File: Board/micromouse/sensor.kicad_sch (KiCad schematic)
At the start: 9 parts, among them Q1 DMN63D8L-7

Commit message: レビュー対応
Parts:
- C4: value 0.1u -> 0.01u
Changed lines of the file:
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@@
       (effects (font (size 1.27 1.27)))
     )
-    (property "Value" "0.1u" (at 163.83 93.98 90)
+    (property "Value" "0.01u" (at 163.83 93.98 90)
       (effects (font (size 1.27 1.27)))
     )

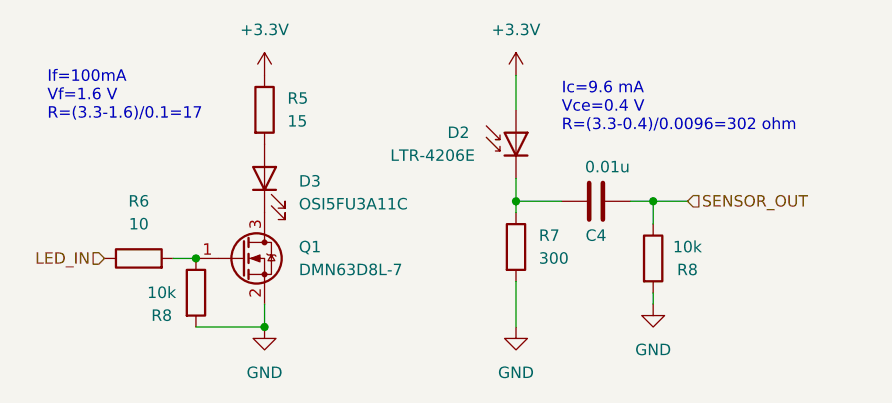
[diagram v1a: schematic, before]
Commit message: 部品型番、URLを追加
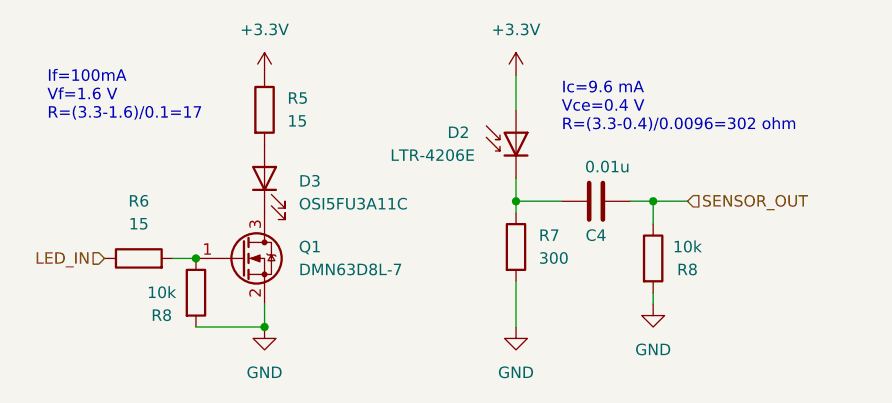
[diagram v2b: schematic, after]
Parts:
- C4: manf# (none) -> GCM155R71H103KA55D; order_URL (none) -> https://www.digikey.jp/ja/products/detail/murata-electronic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
- D2: manf# (none) -> LTR-4206E
- D3: manf# (none) -> OSI5FU3A11C
- R5: manf# (none) -> AC0402FR-0715RL; order_URL (none) -> https://www.digikey.jp/ja/products/detail/yageo/AC0402FR-07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
- R6: value 10 -> 15; manf# (none) -> AC0402FR-0715RL; order_URL (none) -> https://www.digikey.jp/ja/products/detail/yageo/AC0402FR-07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
- R7: manf# (none) -> AC0402FR-07300RL; order_URL (none) -> https://www.digikey.jp/ja/products/detail/yageo/AC0402FR-07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
- R8: manf# (none) -> AC0402FR-0710KL; order_URL (none) -> https://www.digikey.jp/ja/products/detail/yageo/AC0402FR-07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
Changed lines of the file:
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@@
+      (effects (font (size 1.27 1.27)) hide)
+    )
+    (property "manf#" "OSI5FU3A11C" (at 125.73 95.25 0)
       (effects (font (size 1.27 1.27)) hide)
     )
@@
       (effects (font (size 1.27 1.27)) hide)
     )
-    (property "order_URL" "" (at 168.91 104.14 0)
+    (property "order_URL" "https://www.digikey.jp/ja/products/detail/yageo/AC0402FR-0710KL/5895030" (at 168.91 104.14 0)
+      (effects (font (size 1.27 1.27)) hide)
+    )
+    (property "manf#" "AC0402FR-0710KL" (at 168.91 104.14 0)
       (effects (font (size 1.27 1.27)) hide)
     )
@@
       (effects (font (size 1.27 1.27)) hide)
     )
+    (property "manf#" "LTR-4206E" (at 153.67 90.17 0)
+      (effects (font (size 1.27 1.27)) hide)
+    )
     (pin "1")
     (pin "2")
@@
       (effects (font (size 1.27 1.27)) hide)
     )
-    (property "order_URL" "" (at 125.73 87.63 0)
+    (property "order_URL" "https://www.digikey.jp/ja/products/detail/yageo/AC0402FR-0715RL/5895088" (at 125.73 87.63 0)
+      (effects (font (size 1.27 1.27)) hide)
+    )
+    (property "manf#" "AC0402FR-0715RL" (at 125.73 87.63 0)
       (effects (font (size 1.27 1.27)) hide)
     )
@@
       (effects (font (size 1.27 1.27)) hide)
     )
-    (property "order_URL" "" (at 153.67 102.87 0)
+    (property "order_URL" "https://www.digikey.jp/ja/products/detail/yageo/AC0402FR-07300RL/5895269" (at 153.67 102.87 0)
+      (effects (font (size 1.27 1.27)) hide)
+    )
+    (property "manf#" "AC0402FR-07300RL" (at 153.67 102.87 0)
       (effects (font (size 1.27 1.27)) hide)
     )
@@
       (effects (font (size 1.27 1.27)) hide)
     )
-    (property "order_URL" "" (at 162.56 97.79 0)
+    (property "order_URL" "https://www.digikey.jp/ja/products/detail/murata-electronics/GCM155R71H103KA55D/1641636" (at 162.56 97.79 0)
+      (effects (font (size 1.27 1.27)) hide)
+    )
+    (property "manf#" "GCM155R71H103KA55D" (at 162.56 97.79 0)
       (effects (font (size 1.27 1.27)) hide)
     )
@@
       (effects (font (size 1.27 1.27)) hide)
     )
-    (property "order_URL" "" (at 118.11 107.95 0)
+    (property "order_URL" "https://www.digikey.jp/ja/products/detail/yageo/AC0402FR-0710KL/5895030" (at 118.11 107.95 0)
+      (effects (font (size 1.27 1.27)) hide)
+    )
+    (property "manf#" "AC0402FR-0710KL" (at 118.11 107.95 0)
       (effects (font (size 1.27 1.27)) hide)
     )
@@
       (effects (font (size 1.27 1.27)))
     )
-    (property "Value" "10" (at 111.76 100.33 90)
+    (property "Value" "15" (at 111.76 100.33 90)
       (effects (font (size 1.27 1.27)))
     )
@@
       (effects (font (size 1.27 1.27)) hide)
     )
-    (property "order_URL" "" (at 111.76 104.14 0)
-      (effects (font (size 1.27 1.27)) hide)
-    )
+    (property "order_URL" "https://www.digikey.jp/ja/products/detail/yageo/AC0402FR-0715RL/5895088" (at 111.76 104.14 0)
+      (effects (font (size 1.27 1.27)) hide)
+    )
+    (property "manf#" "AC0402FR-0715RL" (at 111.76 104.14 0)
+      (effects (font (size 1.27 1.27)) hide)
+    )
